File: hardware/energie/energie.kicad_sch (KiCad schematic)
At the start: 47 parts, among them J1 transfos, J2 Conn_01x05_Pin, J3 linky, J4 Serial, J6 gpio, J7 I2C, J8 power, Q1 BSS123, Q2 BSS123, U1 MCP6006-OT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

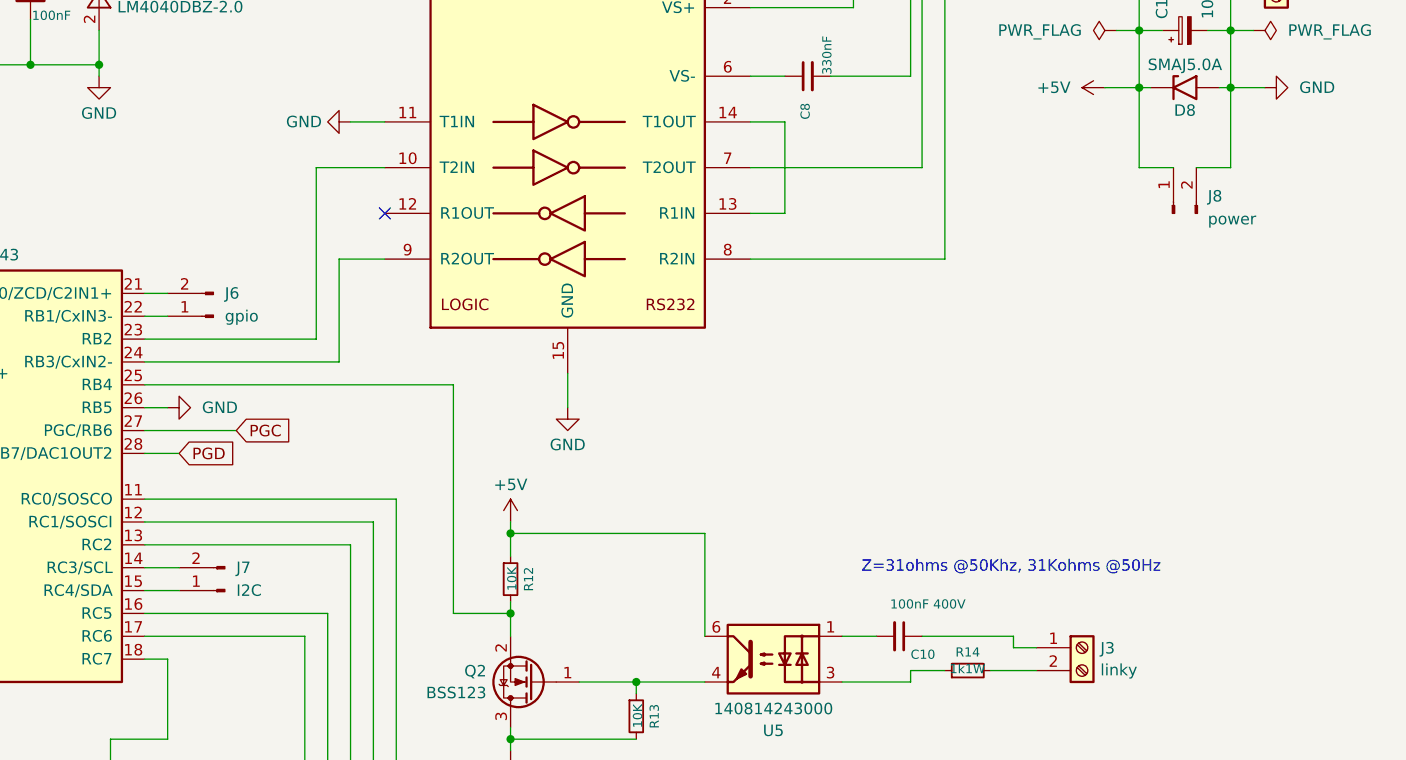
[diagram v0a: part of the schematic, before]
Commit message: energie: ajout d'une alimentation AC/DC pour que le module soit autonome (et que la connection à la centrale puisse être isolée)
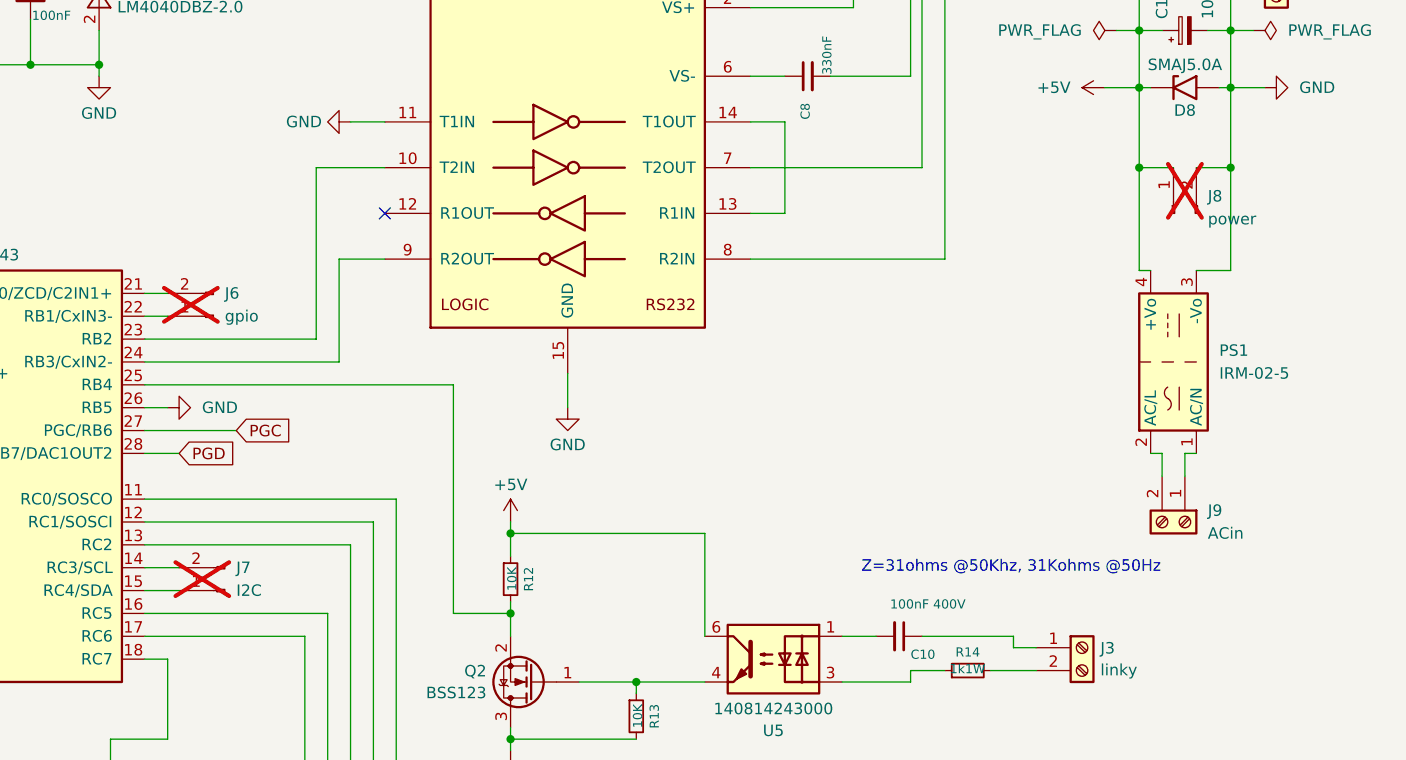
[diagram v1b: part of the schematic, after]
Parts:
- added J9: ACin, Connector_Phoenix_MC:PhoenixContact_MCV_1,5_2-G-3.5_1x02_P3.50mm_Vertical, symbol Connector:Screw_Terminal_01x02
- added PS1: IRM-02-5, Converter_ACDC:Converter_ACDC_MeanWell_IRM-02-xx_THT, symbol Converter_ACDC:IRM-02-5
- J6, J7, J8: now not fitted; now left out of the parts list
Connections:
- net +5V: now also PS1.4 (+Vo)
- net GND: now also PS1.3 (-Vo)
- new net: J9.1 (Pin_1), PS1.1 (AC/N)
- new net: J9.2 (Pin_2), PS1.2 (AC/L)

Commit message: Utilise des emprumtes CMS pour deux connecteurs optionels.
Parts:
- J6, J7: footprint Connector_PinHeader_2.54mm:PinHeader_1x02_P2.54mm_Vertical -> Connector_PinHeader_2.54mm:PinHeader_1x02_P2.54mm_Vertical_SMD_Pin1Left
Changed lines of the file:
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@@
 			)
 		)
-		(property "Footprint" "Connector_PinHeader_2.54mm:PinHeader_1x02_P2.54mm_Vertical"
+		(property "Footprint" "Connector_PinHeader_2.54mm:PinHeader_1x02_P2.54mm_Vertical_SMD_Pin1Left"
 			(at 152.4 116.84 0)
 			(effects
@@
 			)
 		)
-		(property "Footprint" "Connector_PinHeader_2.54mm:PinHeader_1x02_P2.54mm_Vertical"
+		(property "Footprint" "Connector_PinHeader_2.54mm:PinHeader_1x02_P2.54mm_Vertical_SMD_Pin1Left"
 			(at 151.13 86.36 0)
 			(effects

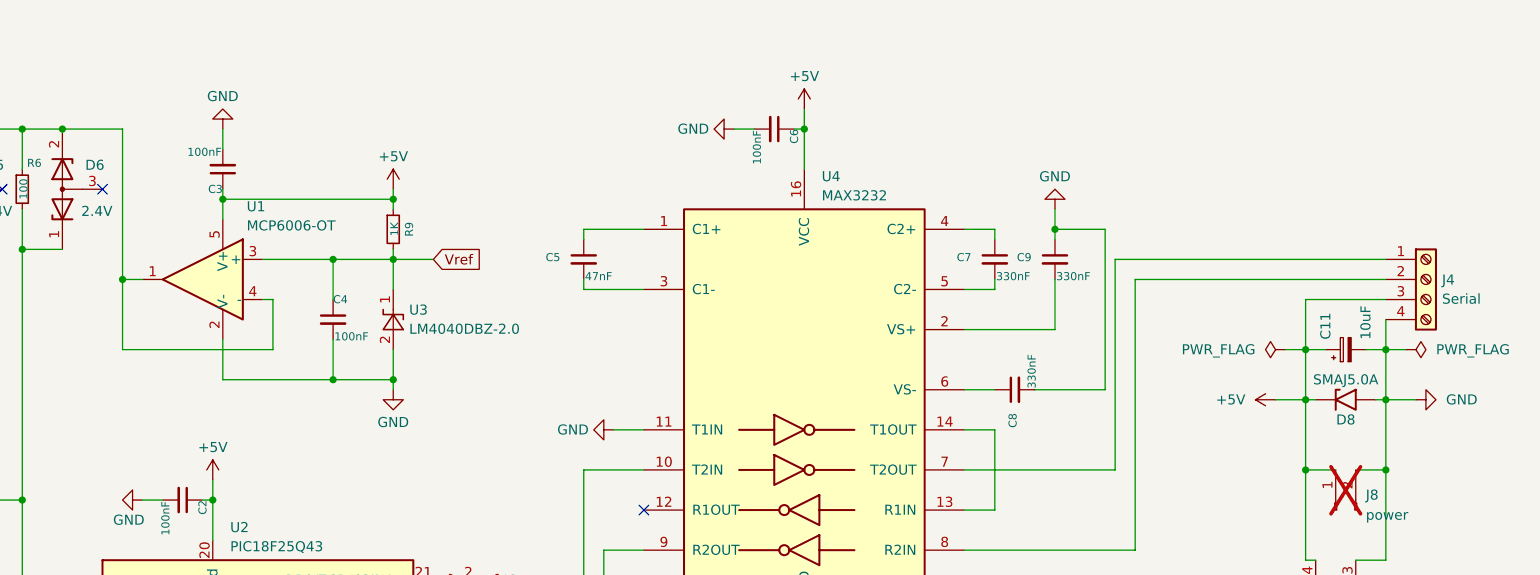
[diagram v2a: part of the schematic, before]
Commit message: Remplace le MCP6006 par MCP6007 que l'on a en stock
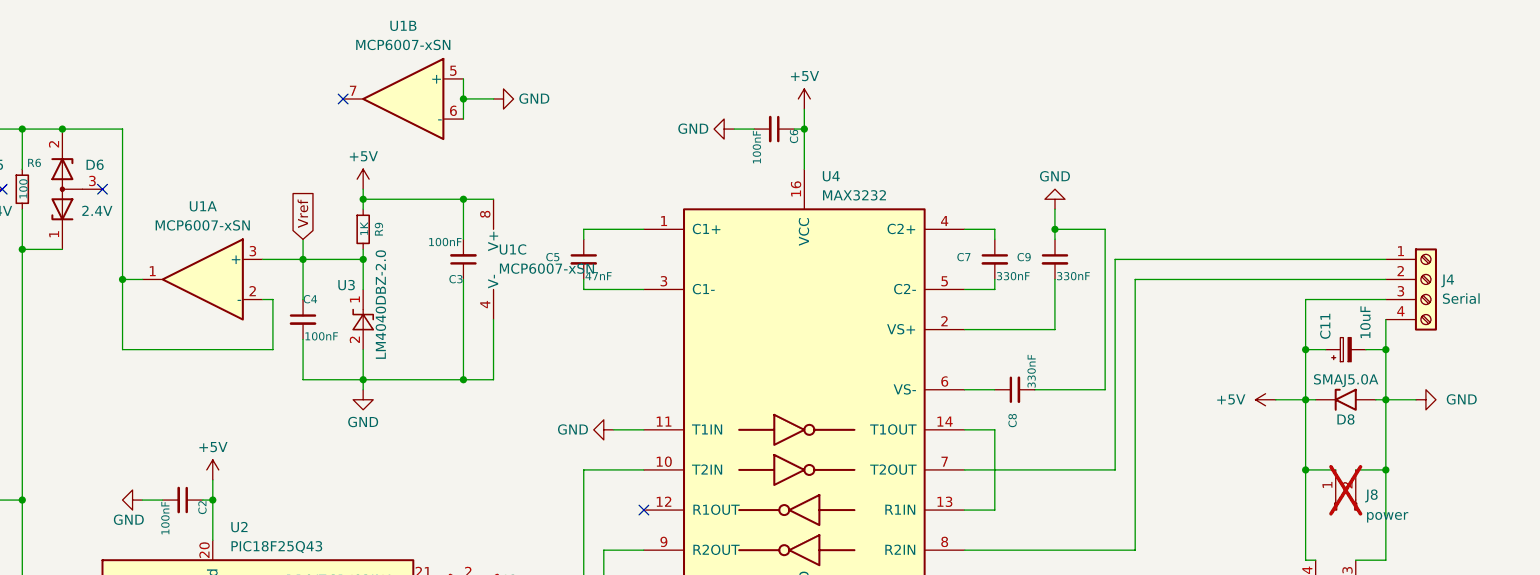
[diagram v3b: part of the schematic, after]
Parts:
- removed U1: MCP6006-OT, Package_TO_SOT_SMD:SOT-23-5, symbol Amplifier_Operational:MCP6001-OT
- added U1: MCP6007-xSN, Package_SO:SOIC-8_3.9x4.9mm_P1.27mm, symbol Amplifier_Operational:MCP6002-xSN
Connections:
- net +5V: now also C3.2, U1.8 (V+); no longer C3.1
- net GND: now also C3.1, U1.4 (V-), U1.5 (+), U1.6 (-); no longer C3.2
- net Vref: now also U1.3 (+)
- net at D1.2 (K), D2.2 (K), D3.2 (K)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: now also U1.1, U1.2 (-)
- no-connect marks 7 -> 8
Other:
- moved on the sheet: C3, C4, R9, U3

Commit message: Remplace BZB984-C2V4 (non dispo) par BZB84-B2V7
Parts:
- D1, D2, D3, D4, D5, D6: value 2.4V -> 2.7V; footprint bouyer-smd.mod:SOT-663 -> Package_TO_SOT_SMD:SOT-23_Handsoldering; P/N BZB984-C2V4 -> BZB84-B2V7
- U5: P/N TLP184(GB-TPL,SE(T -> 140814243000
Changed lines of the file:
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@@
 			)
 		)
-		(property "Value" "2.4V"
+		(property "Value" "2.7V"
 			(at 52.07 37.084 90)
 			(effects
@@
 			)
 		)
-		(property "Footprint" "bouyer-smd.mod:SOT-663"
+		(property "Footprint" "Package_TO_SOT_SMD:SOT-23_Handsoldering"
 			(at 45.72 34.29 0)
 			(effects
@@
 			)
 		)
-		(property "P/N" "BZB984-C2V4"
+		(property "P/N" "BZB84-B2V7"
 			(at 45.72 34.29 0)
 			(effects
@@
 			)
 		)
-		(property "Value" "2.4V"
+		(property "Value" "2.7V"
 			(at 102.87 37.084 90)
 			(effects
@@
 			)
 		)
-		(property "Footprint" "bouyer-smd.mod:SOT-663"
+		(property "Footprint" "Package_TO_SOT_SMD:SOT-23_Handsoldering"
 			(at 96.52 34.29 0)
 			(effects
@@
 			)
 		)
-		(property "P/N" "BZB984-C2V4"
+		(property "P/N" "BZB84-B2V7"
 			(at 96.52 34.29 0)
 			(effects
@@
 			)
 		)
-		(property "Value" "2.4V"
+		(property "Value" "2.7V"
 			(at 90.17 37.084 90)
 			(effects
@@
 			)
 		)
-		(property "Footprint" "bouyer-smd.mod:SOT-663"
+		(property "Footprint" "Package_TO_SOT_SMD:SOT-23_Handsoldering"
 			(at 83.82 34.29 0)
 			(effects
@@
 			)
 		)
-		(property "P/N" "BZB984-C2V4"
+		(property "P/N" "BZB84-B2V7"
 			(at 83.82 34.29 0)
 			(effects
@@
 			)
 		)
-		(property "P/N" "    TLP184(GB-TPL,SE(T"
+		(property "P/N" "140814243000"
 			(at 213.36 124.46 0)
 			(effects
@@
 			)
 		)
-		(property "Value" "2.4V"
+		(property "Value" "2.7V"
 			(at 77.47 37.084 90)
 			(effects
@@
 			)
 		)
-		(property "Footprint" "bouyer-smd.mod:SOT-663"
+		(property "Footprint" "Package_TO_SOT_SMD:SOT-23_Handsoldering"
 			(at 71.12 34.29 0)
 			(effects
@@
 			)
 		)
-		(property "P/N" "BZB984-C2V4"
+		(property "P/N" "BZB84-B2V7"
 			(at 71.12 34.29 0)
 			(effects
@@
 			)
 		)
-		(property "Value" "2.4V"
+		(property "Value" "2.7V"
 			(at 39.37 37.084 90)
 			(effects
@@
 			)
 		)
-		(property "Footprint" "bouyer-smd.mod:SOT-663"
+		(property "Footprint" "Package_TO_SOT_SMD:SOT-23_Handsoldering"
 			(at 33.02 34.29 0)
 			(effects
@@
 			)
 		)
-		(property "P/N" "BZB984-C2V4"
+		(property "P/N" "BZB84-B2V7"
 			(at 33.02 34.29 0)
 			(effects
@@
 			)
 		)
-		(property "Value" "2.4V"
+		(property "Value" "2.7V"
 			(at 64.77 37.084 90)
 			(effects
@@
 			)
 		)
-		(property "Footprint" "bouyer-smd.mod:SOT-663"
+		(property "Footprint" "Package_TO_SOT_SMD:SOT-23_Handsoldering"
 			(at 58.42 34.29 0)
 			(effects
@@
 			)
 		)
-		(property "P/N" "BZB984-C2V4"
+		(property "P/N" "BZB84-B2V7"
 			(at 58.42 34.29 0)
 			(effects

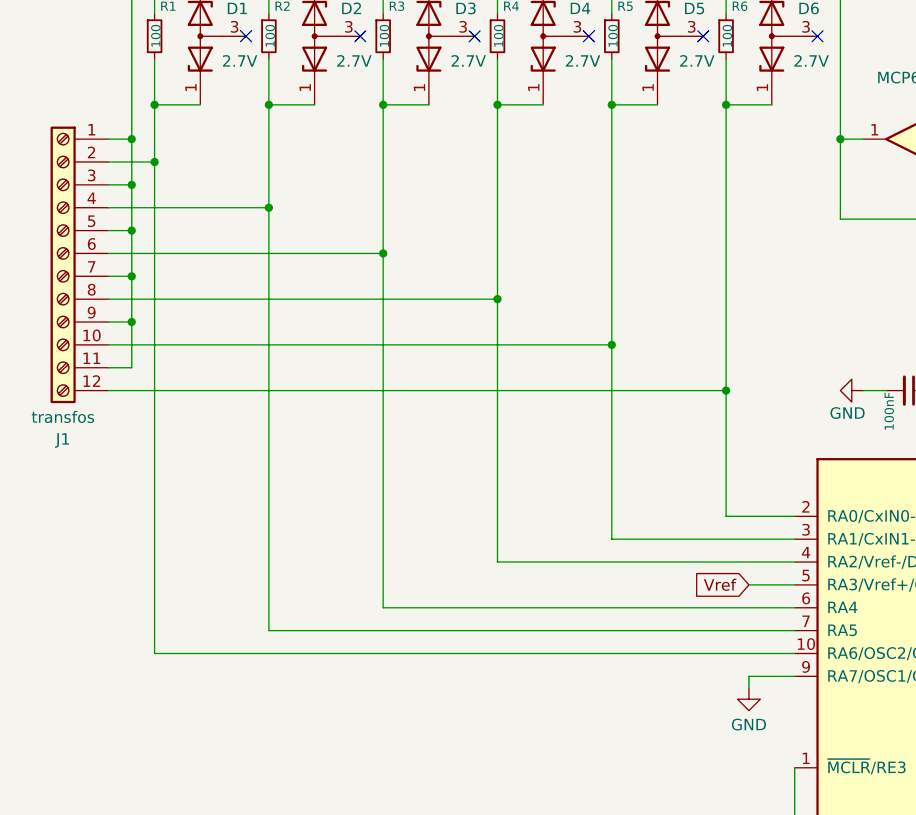
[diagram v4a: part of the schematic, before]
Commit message: Energie: mesure de courant ajout d'une resistance de protection serie sur les entrees pic18
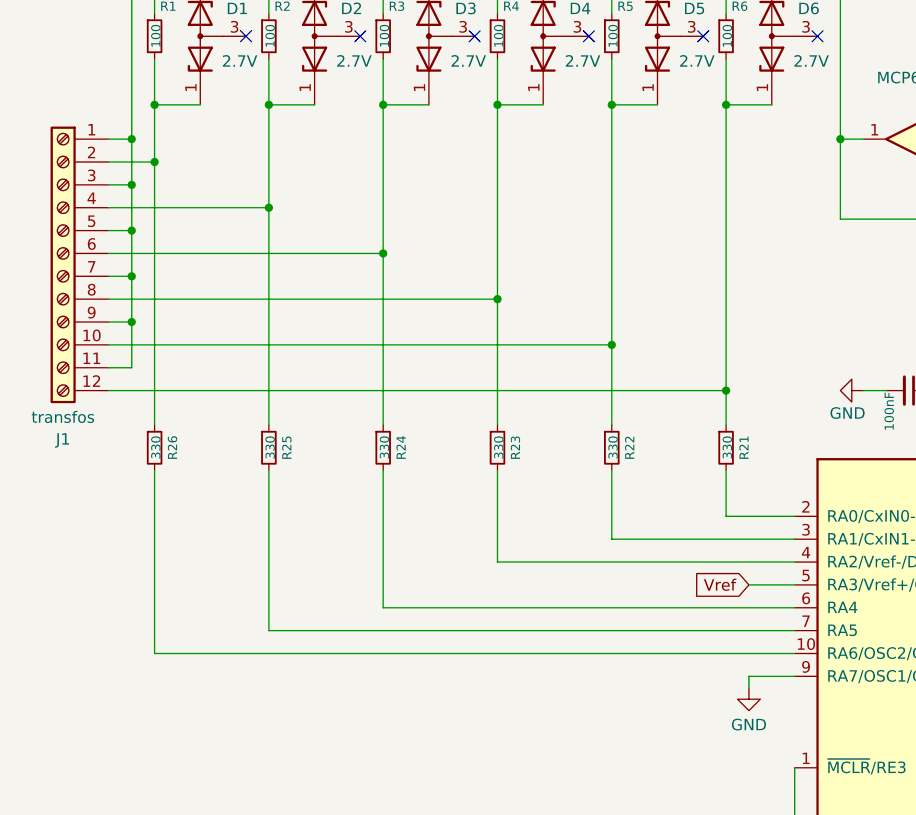
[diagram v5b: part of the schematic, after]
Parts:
- added R21, R22, R23, R24, R25, R26: 330, Resistor_SMD:R_0805_2012Metric_Pad1.20x1.40mm_HandSolder, symbol Device:R_Small
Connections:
- net at D2.1 (K), J1.4 (Pin_4), R2.2: now also R25.1; no longer U2.7 (RA5)
- net at D1.1 (K), J1.2 (Pin_2), R1.2: now also R26.1; no longer U2.10 (RA6/OSC2/CLKOUT)
- net at D6.1 (K), J1.12 (Pin_12), R6.2: now also R21.1; no longer U2.2 (RA0/CxIN0-)
- net at D5.1 (K), J1.10 (Pin_10), R5.2: now also R22.1; no longer U2.3 (RA1/CxIN1-)
- net at D4.1 (K), J1.8 (Pin_8), R4.2: now also R23.1; no longer U2.4 (RA2/Vref-/DAC1OUT1/CxIN0+)
- net at D3.1 (K), J1.6 (Pin_6), R3.2: now also R24.1; no longer U2.6 (RA4)
- new net: R26.2, U2.10 (RA6/OSC2/CLKOUT)
- new net: R21.2, U2.2 (RA0/CxIN0-)
- new net: R22.2, U2.3 (RA1/CxIN1-)
- new net: R23.2, U2.4 (RA2/Vref-/DAC1OUT1/CxIN0+)
- new net: R24.2, U2.6 (RA4)
- new net: R25.2, U2.7 (RA5)

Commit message: Adjust some references and availability
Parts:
- C10: P/N C1808X104KBRAC -> C1808V104KBRACTU
- D7: P/N APT1608EC -> APT1608EC (stock)
- PS1: value IRM-02-5 -> IRM-01-5; P/N (none) -> IRM-01-5
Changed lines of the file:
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@@
 			)
 		)
-		(property "P/N" "APT1608EC"
+		(property "P/N" "APT1608EC (stock)"
 			(at 147.32 170.18 0)
 			(effects
@@
 			)
 		)
-		(property "P/N" "C1808X104KBRAC"
+		(property "P/N" " C1808V104KBRACTU"
 			(at 227.33 121.92 90)
 			(effects
@@
 			)
 		)
-		(property "Value" "IRM-02-5"
+		(property "Value" "IRM-01-5"
 			(at 262.89 92.7099 90)
 			(effects
@@
 			(effects
 				(font
+					(size 1.27 1.27)
+				)
+				(hide yes)
+			)
+		)
+		(property "P/N" "IRM-01-5"
+			(at 257.81 91.44 90)
+			(effects
+				(font

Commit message: Fix Q2 wiring, it was reversed Fix U5 footprint Fix C10 and similar footprints
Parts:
- C10: footprint Capacitor_SMD:C_1812_4532Metric -> local:C_1808_4520Metric_Pad1.72x2.30mm_HandSolder
- U5: footprint Package_SO:MFSOP6-4_4.4x3.6mm_P1.27mm -> Package_DIP:SMDIP-4_W9.53mm; symbol Isolator:TLP184 -> Isolator:TLP290
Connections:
- net +5V: now also U5.4; no longer U5.6
- net GND: now also Q2.2 (S); no longer Q2.3 (D)
- net at R12.2, U2.25 (RB4): now also Q2.3 (D); no longer Q2.2 (S)
- net at R14.1: now also U5.2; no longer U5.3
- net at Q2.1 (G), R13.1: now also U5.3; no longer U5.4
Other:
- moved on the sheet: Q2
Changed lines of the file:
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@@
 			)
 		)
-		(property "Footprint" "Capacitor_SMD:C_1812_4532Metric"
+		(property "Footprint" "local:C_1808_4520Metric_Pad1.72x2.30mm_HandSolder"
 			(at 223.52 122.8852 0)
 			(effects
@@
 	)
 	(symbol
-		(lib_id "Isolator:TLP184")
+		(lib_id "Isolator:TLP290")
 		(at 213.36 124.46 0)
 		(mirror y)
@@
 			)
 		)
-		(property "Footprint" "Package_SO:MFSOP6-4_4.4x3.6mm_P1.27mm"
-			(at 213.36 132.08 0)
+		(property "Footprint" "Package_DIP:SMDIP-4_W9.53mm"
+			(at 234.95 129.54 0)
 			(effects
 				(font
@@
 					(italic yes)
 				)
-				(hide yes)
-			)
-		)
-		(property "Datasheet" "https://toshiba.semicon-storage.com/info/docget.jsp?did=11793&prodName=TLP184"
-			(at 212.09 124.46 0)
-			(effects
-				(font
-					(size 1.27 1.27)
-				)
 				(justify left)
 				(hide yes)
 			)
 		)
-		(property "Description" "AC/DC Optocoupler, Vce 80V, CTR 50-100%, MFSOP6"
+		(property "Datasheet" "https://toshiba.semicon-storage.com/info/docget.jsp?did=12882&prodName=TLP290"
+			(at 212.725 124.46 0)
+			(effects
+				(font
+					(size 1.27 1.27)
+				)
+				(justify left)
+				(hide yes)
+			)
+		)
+		(property "Description" "AC/DC Phototransistor Optocoupler, Vce 80V, CTR 50-600%, not recommended for new designs, SOP4"
 			(at 213.36 124.46 0)
 			(effects
@@
 		(pin "3"
 		)
-		(pin "6"
+		(pin "2"
 		)
 		(pin "1"
@@
 	(symbol
 		(lib_id "Transistor_FET:BSS123")
-		(at 186.69 127 180)
-		(unit 1)
-		(exclude_from_sim no)
-		(in_bom yes)
-		(on_board yes)
-		(dnp no)
-		(fields_autoplaced yes)
+		(at 186.69 127 0)
+		(mirror y)
+		(unit 1)
+		(exclude_from_sim no)
+		(in_bom yes)
+		(on_board yes)
+		(dnp no)
 		(property "Reference" "Q2"
-			(at 181.4831 125.7878 0)
+			(at 181.4831 128.2122 0)
 			(effects
 				(font
@@
 		)
 		(property "Value" "BSS123"
-			(at 181.4831 128.2121 0)
+			(at 181.4831 125.7879 0)
 			(effects
 				(font
@@
 		)
 		(property "Footprint" "Package_TO_SOT_SMD:SOT-23"
-			(at 181.61 125.095 0)
+			(at 181.61 128.905 0)
 			(effects
 				(font
@@
 		)
 		(property "Datasheet" "http://www.diodes.com/assets/Datasheets/ds30366.pdf"
-			(at 181.61 123.19 0)
-			(effects
-				(font
+			(at 181.61 130.81 0)
+			(effects
+				(font

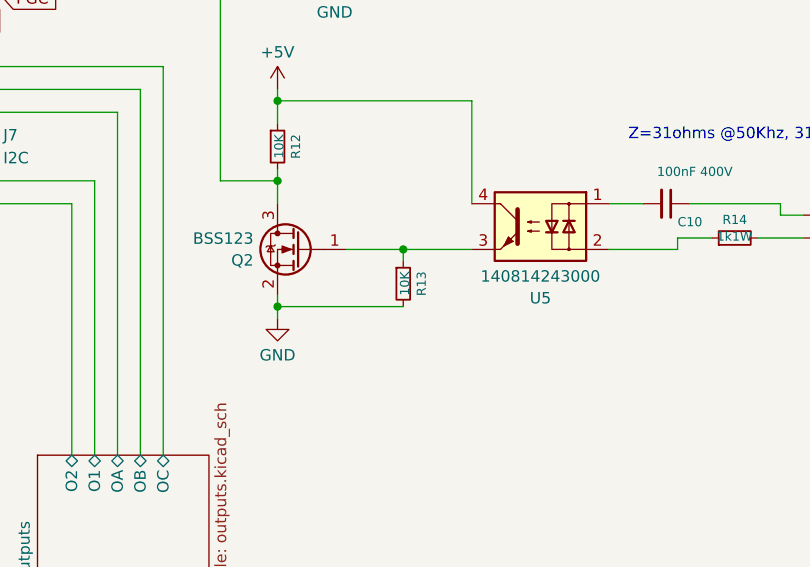
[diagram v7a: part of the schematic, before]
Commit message: linky interface: update gate resitor value after tests
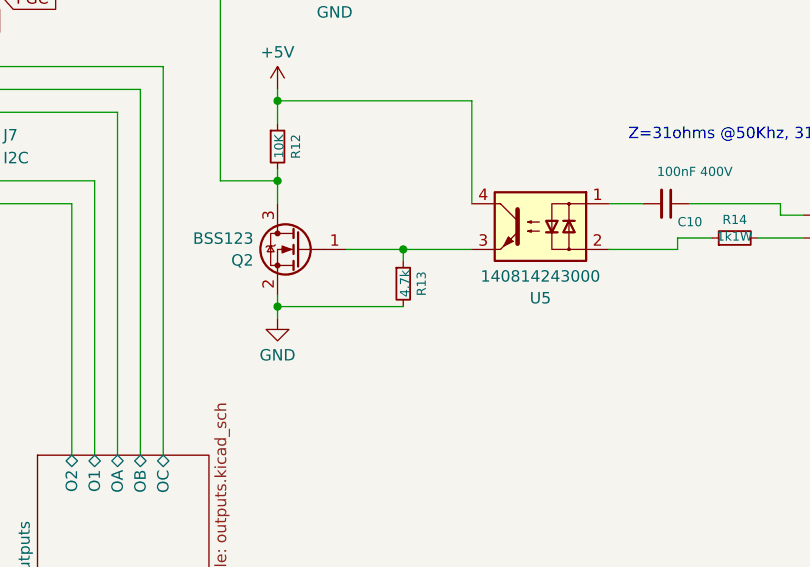
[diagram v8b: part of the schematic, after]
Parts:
- R13: value 10K -> 4.7k
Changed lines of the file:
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@@
 			)
 		)
-		(property "Value" "10K"
+		(property "Value" "4.7k"
 			(at 198.2978 130.7846 90)
 			(effects
